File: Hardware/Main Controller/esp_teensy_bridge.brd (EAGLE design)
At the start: 99.7 x 88.3 mm, 47 parts, among them IC1 BQ79600PWRQ1, Q1 SI7611DN-T1-GE3, Q2 SI7611DN-T1-GE3, Q3 SI7611DN-T1-GE3, Q4 SI7611DN-T1-GE3

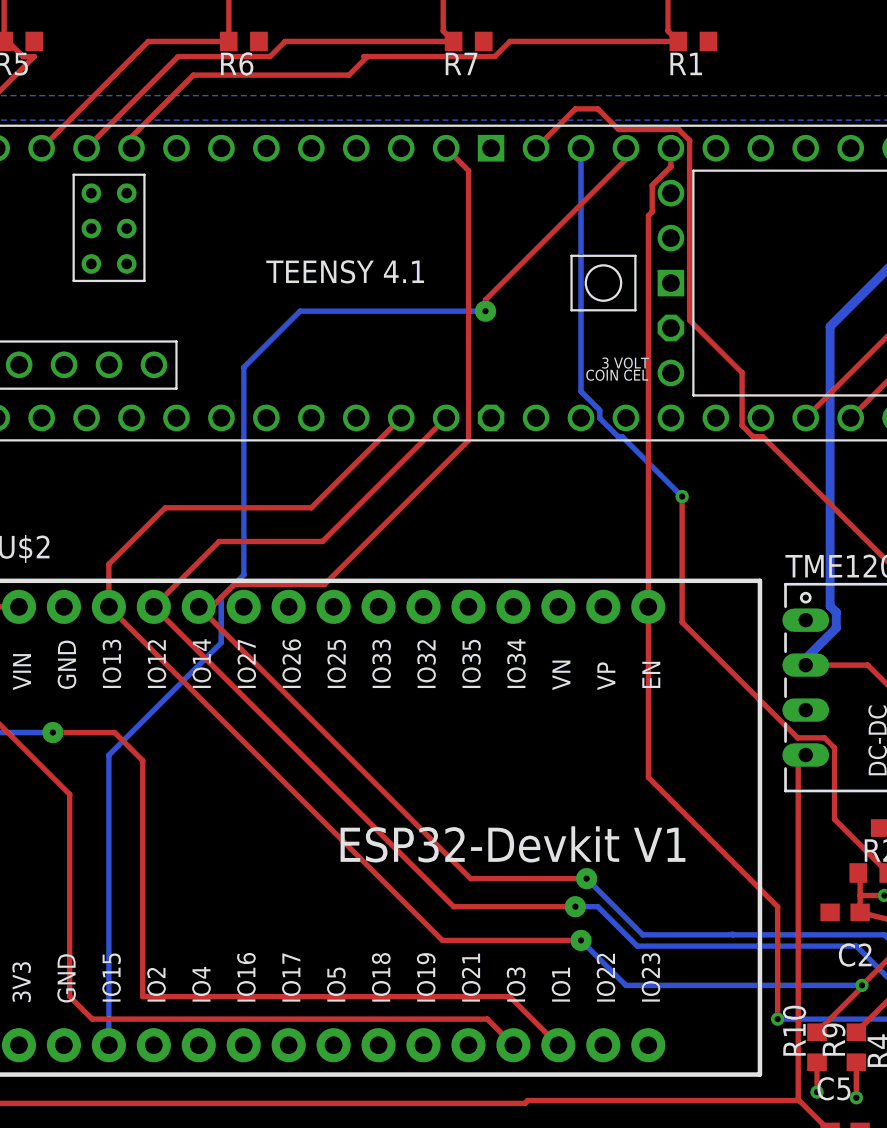
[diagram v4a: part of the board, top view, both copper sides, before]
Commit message: seperate spi
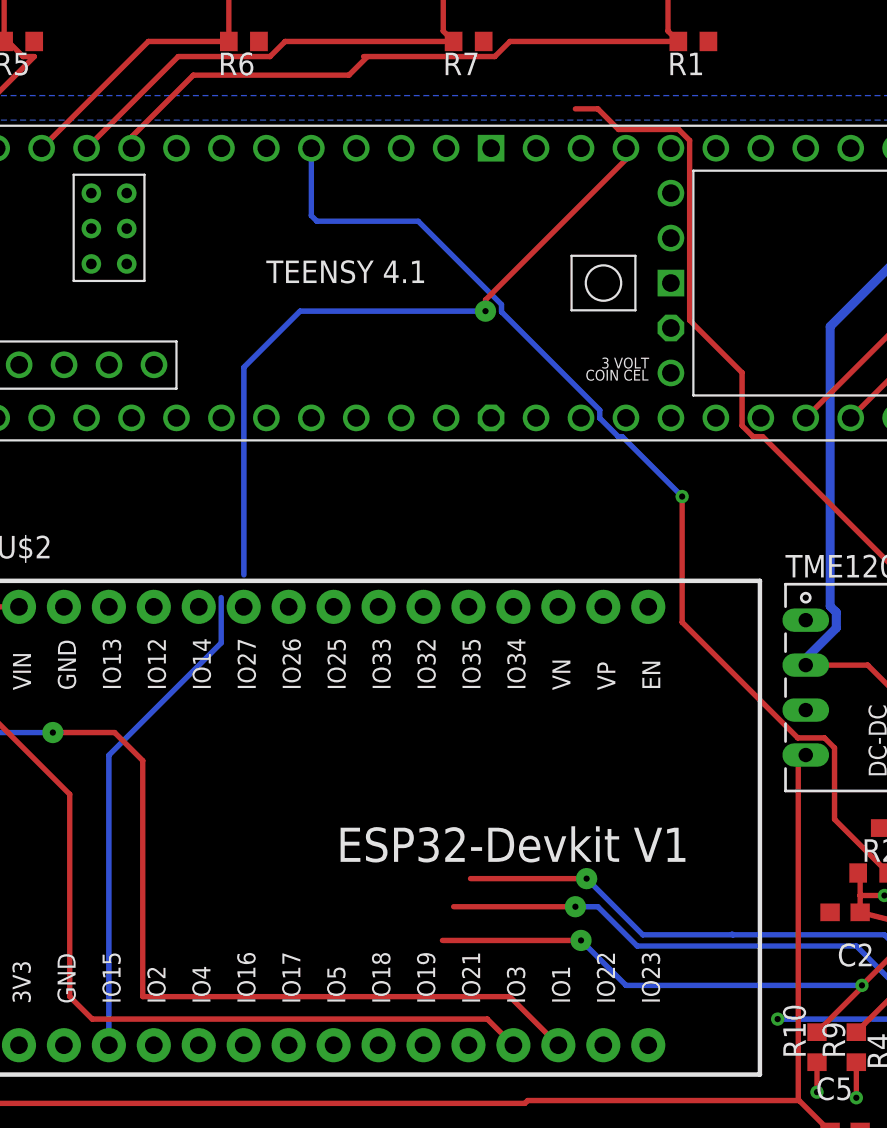
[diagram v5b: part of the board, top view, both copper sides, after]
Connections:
- removed net RX_BRIDGE: U$3.29-TX7
- removed net TX_BRIDGE: U$3.28-RX7
- new net MISO_ESP: U$2.27, U$3.41-A17/MISO1
- new net MOSI_ESP: U$2.28, U$3.26-A12/MOSI1
- new net SCK_ESP: U$2.26, U$3.27-A13/SCK1
- net MISO: no longer U$2.27
- net MOSI: no longer U$2.28
- net NFAULT: now also U$3.16-A2/RX4/SCL1; no longer U$3.40-A16/CS1
- net SCK: no longer U$2.26
- net SPI_RDY: now also U$3.17-A3/TX4/SDA1; no longer U$3.41-A17/MISO1
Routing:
- net SCK: track 87.8 -> 29.9 mm
- net CS0: track 66.1 -> 13.3 mm
- net MOSI: track 84.2 -> 35.1 mm
- net MISO: track 80.5 -> 35.6 mm
- net NFAULT: track 54.4 -> 64.0 mm
- net SPI_RDY: track 68.0 -> 64.8 mm
- net CS1: track 68.9 -> 67.1 mm
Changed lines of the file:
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@@
 <wire x1="14.9225" y1="13.335" x2="37.25" y2="13.335" width="0.3048" layer="1"/>
-</signal>
-<signal name="TX_BRIDGE">
-<contactref element="U$3" pad="28-RX7"/>
-</signal>
-<signal name="RX_BRIDGE">
-<contactref element="U$3" pad="29-TX7"/>
 </signal>
 <signal name="5V">
@@
 <contactref element="IC1" pad="4"/>
 <contactref element="U$3" pad="11-MOSI/CTX1"/>
-<contactref element="U$2" pad="28"/>
 <via x="58.42" y="15.24" extent="1-16" drill="0.35"/>
 <wire x1="58.42" y1="15.24" x2="60.9675" y2="17.7875" width="0.3048" layer="1"/>
@@
 <wire x1="55.88" y1="12.5975" x2="58.42" y2="15.1375" width="0.3048" layer="1"/>
 <wire x1="58.42" y1="15.1375" x2="58.42" y2="15.24" width="0.3048" layer="1"/>
-<wire x1="32.385" y1="47.3075" x2="27.305" y2="42.2275" width="0.3048" layer="1"/>
-<wire x1="27.305" y1="42.2275" x2="19.05" y2="42.2275" width="0.3048" layer="1"/>
-<wire x1="19.05" y1="42.2275" x2="15.865" y2="39.0425" width="0.3048" layer="1"/>
-<wire x1="15.865" y1="39.0425" x2="15.865" y2="36.63" width="0.3048" layer="1"/>
 <wire x1="45.085" y1="15.24" x2="42.545" y2="17.78" width="0.3048" layer="16"/>
 <via x="42.545" y="17.78" extent="1-16" drill="0.35" diameter="1.2"/>
-<wire x1="34.715" y1="17.78" x2="15.865" y2="36.63" width="0.3048" layer="1"/>
 <wire x1="58.42" y1="15.24" x2="45.085" y2="15.24" width="0.3048" layer="16"/>
 <wire x1="42.545" y1="17.78" x2="34.715" y2="17.78" width="0.3048" layer="1"/>
+<wire x1="34.715" y1="17.78" x2="32.385" y2="47.3075" width="0" layer="19" extent="1-1"/>
 </signal>
 <signal name="MISO">
 <contactref element="IC1" pad="5"/>
 <contactref element="U$3" pad="12-MISO/MQSL"/>
-<contactref element="U$2" pad="27"/>
 <wire x1="60.325" y1="15.24" x2="58.1025" y2="17.4625" width="0.3048" layer="16"/>
 <via x="60.325" y="15.24" extent="1-16" drill="0.35"/>
@@
 <via x="42.2275" y="19.685" extent="1-16" drill="0.35" diameter="1.2"/>
 <wire x1="42.2275" y1="19.685" x2="35.35" y2="19.685" width="0.3048" layer="1"/>
-<wire x1="35.35" y1="19.685" x2="18.405" y2="36.63" width="0.3048" layer="1"/>
-<wire x1="18.405" y1="36.63" x2="22.0975" y2="40.3225" width="0.3048" layer="1"/>
-<wire x1="22.0975" y1="40.3225" x2="27.94" y2="40.3225" width="0.3048" layer="1"/>
-<wire x1="27.94" y1="40.3225" x2="34.925" y2="47.3075" width="0.3048" layer="1"/>
+<wire x1="35.35" y1="19.685" x2="34.925" y2="47.3075" width="0" layer="19" extent="1-1"/>
 </signal>
 <signal name="SCK">
 <contactref element="IC1" pad="6"/>
 <contactref element="U$3" pad="13-SCK/LED"/>
-<contactref element="U$2" pad="26"/>
 <wire x1="51.0829125" y1="18.1455" x2="51.1309125" y2="18.0975" width="0.3048" layer="16"/>
 <wire x1="59.69" y1="18.0975" x2="61.2775" y2="16.51" width="0.3048" layer="16"/>
@@
 <via x="42.8625" y="21.2725" extent="1-16" drill="0.35" diameter="1.2"/>
 <wire x1="42.8625" y1="21.2725" x2="36.3025" y2="21.2725" width="0.3048" layer="1"/>
-<wire x1="36.3025" y1="21.2725" x2="20.945" y2="36.63" width="0.3048" layer="1"/>
 <wire x1="46.0375" y1="18.0975" x2="42.8625" y2="21.2725" width="0.3048" layer="16"/>
-<wire x1="28.0575" y1="37.9" x2="36.195" y2="46.0375" width="0.3048" layer="1"/>
-<wire x1="20.945" y1="36.63" x2="21.68894375" y2="36.63" width="0.3048" layer="1"/>
-<wire x1="21.68894375" y1="36.63" x2="22.95894375" y2="37.9" width="0.3048" layer="1"/>
-<wire x1="22.95894375" y1="37.9" x2="28.0575" y2="37.9" width="0.3048" layer="1"/>
-<wire x1="36.195" y1="46.0375" x2="36.195" y2="61.2775" width="0.3048" layer="1"/>
-<wire x1="36.195" y1="61.2775" x2="34.925" y2="62.5475" width="0.3048" layer="1"/>
+<wire x1="36.3025" y1="21.2725" x2="34.925" y2="62.5475" width="0" layer="19" extent="1-1"/>
 </signal>
 <signal name="CS1">
@@
 <via x="37.1475" y="53.34" extent="1-16" drill="0.35" diameter="1.2"/>
 <wire x1="37.1475" y1="53.34" x2="26.67" y2="53.34" width="0.3048" layer="16"/>
-<wire x1="23.495" y1="38.43605625" x2="22.215" y2="37.15605625" width="0.3048" layer="16"/>
 <wire x1="22.215" y1="37.15605625" x2="22.215" y2="34.5975" width="0.3048" layer="16"/>
 <wire x1="15.865" y1="28.2475" x2="15.865" y2="11.86" width="0.3048" layer="16"/>
@@
 <wire x1="23.495" y1="50.165" x2="23.495" y2="38.43605625" width="0.3048" layer="16"/>
 <wire x1="22.215" y1="34.5975" x2="15.865" y2="28.2475" width="0.3048" layer="16"/>
+<wire x1="22.215" y1="37.15605625" x2="23.495" y2="38.43605625" width="0" layer="19" extent="16-16"/>
 </signal>
 <signal name="CS0">
 <contactref element="U$3" pad="38-A14/CS/IN1"/>
 <contactref element="IC1" pad="7"/>
-<wire x1="47.625" y1="62.5475" x2="47.625" y2="61.504875" width="0.3048" layer="1"/>
-<wire x1="46.5662" y1="58.9487" x2="46.355" y2="58.7375" width="0.3048" layer="1"/>
-<wire x1="47.625" y1="61.504875" x2="46.5662" y2="60.446075" width="0.3048" layer="1"/>
-<wire x1="46.5662" y1="60.446075" x2="46.5662" y2="58.9487" width="0.3048" layer="1"/>
-<wire x1="46.355" y1="58.7375" x2="46.355" y2="26.9875" width="0.3048" layer="1"/>
-<wire x1="46.355" y1="26.9875" x2="53.6575" y2="19.685" width="0.3048" layer="1"/>
-<wire x1="53.6575" y1="19.685" x2="53.6575" y2="13.335" width="0.3048" layer="1"/>
 <via x="53.6575" y="13.335" extent="1-16" drill="0.35"/>
 <wire x1="53.6575" y1="13.335" x2="61.2775" y2="13.335" width="0.3048" layer="16"/>
@@
 <wire x1="60.6425" y1="11.9625" x2="60.6425" y2="12.7" width="0.3048" layer="1"/>
 <wire x1="60.6425" y1="12.7" x2="61.2775" y2="13.335" width="0.3048" layer="1"/>
+<wire x1="64.0545" y1="15.8375" x2="47.625" y2="62.5475" width="0" layer="19" extent="1-1"/>
 </signal>
 <signal name="NFAULT">
@@
 <wire x1="64.0545" y1="19.0875" x2="62.4075" y2="19.0875" width="0.3048" layer="1"/>
 <wire x1="62.4075" y1="19.0875" x2="59.905" y2="21.59" width="0.3048" layer="1"/>
-<contactref element="U$3" pad="40-A16/CS1"/>
 <via x="48.26" y="42.8625" extent="1-16" drill="0.35"/>
 <wire x1="56.8706" y1="28.6573" x2="56.3052" y2="29.2227" width="0.3048" layer="1"/>
@@
 <wire x1="48.26" y1="42.8625" x2="44.8738" y2="46.2487" width="0.3048" layer="16"/>
 <wire x1="44.8738" y1="46.2487" x2="44.646425" y2="46.2487" width="0.3048" layer="16"/>
-<wire x1="42.545" y1="48.804875" x2="42.545" y2="62.5475" width="0.3048" layer="16"/>
-<wire x1="43.6038" y1="47.746075" x2="42.545" y2="48.804875" width="0.3048" layer="16"/>
 <wire x1="44.646425" y1="46.2487" x2="43.6038" y2="47.291325" width="0.3048" layer="16"/>
 <wire x1="43.6038" y1="47.291325" x2="43.6038" y2="47.746075" width="0.3048" layer="16"/>
+<contactref element="U$3" pad="16-A2/RX4/SCL1"/>
+<wire x1="38.0523" y1="53.297575" x2="38.0523" y2="53.71478125" width="0.3048" layer="16"/>
+<wire x1="38.0523" y1="53.71478125" x2="33.34708125" y2="58.42" width="0.3048" layer="16"/>
+<wire x1="33.34708125" y1="58.42" x2="27.6225" y2="58.42" width="0.3048" layer="16"/>
+<wire x1="27.6225" y1="58.42" x2="27.305" y2="58.7375" width="0.3048" layer="16"/>
+<wire x1="27.305" y1="58.7375" x2="27.305" y2="62.5475" width="0.3048" layer="16"/>
+<wire x1="43.6038" y1="47.746075" x2="38.0523" y2="53.297575" width="0.3048" layer="16"/>
 </signal>
 <signal name="SPI_RDY">
@@
 <wire x1="63.5" y1="13.55" x2="63.5" y2="14.633" width="0.3048" layer="1"/>
 <wire x1="63.5" y1="14.633" x2="64.0545" y2="15.1875" width="0.3048" layer="1"/>
-<contactref element="U$3" pad="41-A17/MISO1"/>
 <wire x1="64.91825" y1="15.3077" x2="65.0968" y2="15.48625" width="0.3048" layer="1"/>
 <wire x1="62.6041" y1="35.0222125" x2="62.6041" y2="36.4559" width="0.3048" layer="1"/>
@@
 <wire x1="48.063575" y1="63.6063" x2="44.6612" y2="63.6063" width="0.3048" layer="1"/>
 <wire x1="43.4975" y1="64.77" x2="42.2275" y2="64.77" width="0.3048" layer="1"/>
-<wire x1="42.2275" y1="64.77" x2="40.005" y2="62.5475" width="0.3048" layer="1"/>
 <wire x1="62.6041" y1="36.4559" x2="52.8113" y2="46.2487" width="0.3048" layer="1"/>
+<contactref element="U$3" pad="17-A3/TX4/SDA1"/>
+<wire x1="42.2275" y1="64.77" x2="24.765" y2="62.5475" width="0" layer="19" extent="1-1"/>
+</signal>
+<signal name="MOSI_ESP">
+<contactref element="U$3" pad="26-A12/MOSI1"/>
+<contactref element="U$2" pad="28"/>
+<wire x1="15.865" y1="36.63" x2="45.085" y2="47.3075" width="0" layer="19" extent="1-1"/>
+</signal>
+<signal name="MISO_ESP">
+<contactref element="U$3" pad="41-A17/MISO1"/>
+<contactref element="U$2" pad="27"/>
+<wire x1="18.405" y1="36.63" x2="40.005" y2="62.5475" width="0" layer="19" extent="1-1"/>
+</signal>
+<signal name="SCK_ESP">
+<contactref element="U$3" pad="27-A13/SCK1"/>
+<contactref element="U$2" pad="26"/>
+<wire x1="20.945" y1="36.63" x2="47.625" y2="47.3075" width="0" layer="19" extent="1-1"/>
 </signal>
 </signals>

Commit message: 1/19/2022 changes josh/isaac
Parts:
- moved PWR_IN 23.6 mm to (61.6, 81.3)
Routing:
- net CS0: track 13.3 -> 65.9 mm
- net SCK: track 29.9 -> 77.3 mm, vias 2 -> 4
- net SCK_ESP: track 0.00 -> 38.8 mm, vias 0 -> 1
- net MISO_ESP: track 0.00 -> 35.6 mm, vias 0 -> 1
- net MOSI_ESP: track 0.00 -> 33.8 mm, vias 0 -> 3
- net GND: track 0.00 -> 31.2 mm, vias 0 -> 5
- net MOSI: track 35.1 -> 65.6 mm
- net MISO: track 35.6 -> 63.3 mm
- net VCC: track 143.0 -> 115.3 mm
- net SPI_RDY: track 64.8 -> 83.2 mm
- net CS1: track 67.1 -> 68.9 mm

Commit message: final additions hopefully
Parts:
- added LED1, LED2, LED3, LED4, LED5, LED6, LED7, LED8: (no value), led:SML0603
- added R11, R12, R13, R14: 100k, rcl:R0603
- added R15, R16, R17, R18: 50, rcl:R0603
- added X1: 5566-12, con-molex:5566-12
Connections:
- new net N$13: LED4.A, R14.2
- new net N$14: U$3.14-A0/TX3/SPDIF_OUT, X1.1
- new net N$17: U$3.15-A1/RX3/SPDIF_IN, X1.2
- new net N$18: U$3.18-A4/SDA0, X1.3
- new net N$19: U$3.19-A5/SCL0, X1.4
- new net N$20: U$3.24-A10/TX6/SCL2, X1.5
- new net N$21: U$3.25-A11/RX6/SDA2, X1.6
- new net N$22: U$3.40-A16/CS1, X1.7
- new net N$23: U$3.32-OUT1B, X1.8
- new net N$24: U$3.9-OUT1C, X1.9
- new net N$25: U$3.6-OUT1D, X1.10
- new net N$26: U$3.33-MCLK2, X1.12
- new net N$27: U$3.2-OUT2, X1.11
- new net N$28: R15.1, U$2.10
- new net N$29: R16.1, U$2.9
- new net N$3: LED1.A, R11.2
- new net N$30: R17.1, U$2.8
- new net N$31: R18.1, U$2.7
- new net N$32: LED5.A, R15.2
- new net N$33: LED6.A, R16.2
- new net N$34: LED7.A, R17.2
- new net N$35: LED8.A, R18.2
- new net N$4: LED2.A, R12.2
- new net N$9: LED3.A, R13.2
- net GND: now also LED1.C, LED2.C, LED3.C, LED4.C, LED5.C, LED6.C, LED7.C, LED8.C
- net N$12: now also R12.1
- net N$2: now also R13.1
- net N$5: now also R14.1
- net N$6: now also R11.1
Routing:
- net N$27: track 0.00 -> 89.1 mm, vias 0 -> 4
- net N$25: track 0.00 -> 71.5 mm, vias 0 -> 6
- net N$20: track 0.00 -> 70.9 mm, vias 0 -> 2
- net N$19: track 0.00 -> 69.8 mm
- net N$21: track 0.00 -> 66.1 mm, vias 0 -> 2
- net N$18: track 0.00 -> 62.3 mm
- net N$24: track 0.00 -> 58.9 mm, vias 0 -> 3
- net N$17: track 0.00 -> 49.1 mm, vias 0 -> 1
- net N$14: track 0.00 -> 41.6 mm, vias 0 -> 1
- net N$26: track 0.00 -> 39.9 mm
- net N$22: track 0.00 -> 31.3 mm, vias 0 -> 1
- net N$23: track 0.00 -> 23.9 mm
- net N$31: track 0.00 -> 5.93 mm, vias 0 -> 1
- net N$30: track 0.00 -> 5.93 mm, vias 0 -> 1
- net N$29: track 0.00 -> 5.93 mm, vias 0 -> 1
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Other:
- board text added: "CAN"
- board text added: "COMH"
- board text added: "COML"

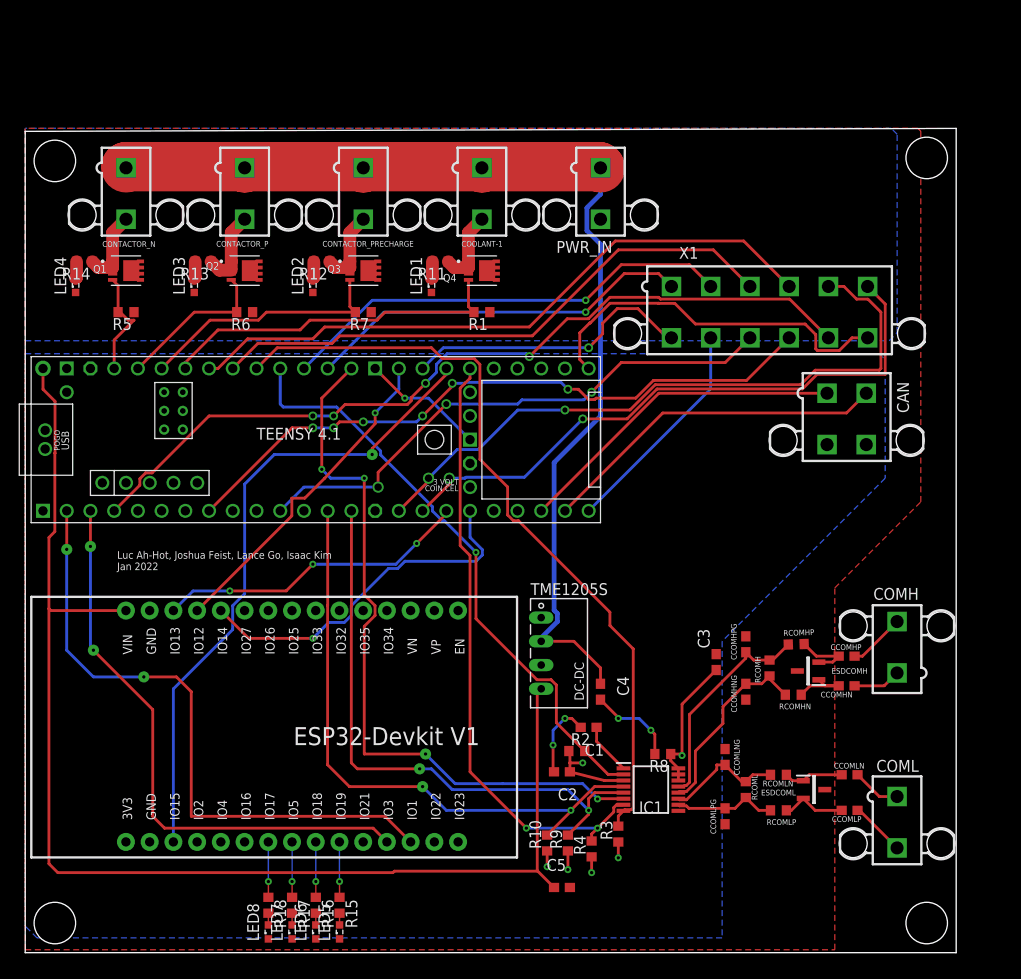
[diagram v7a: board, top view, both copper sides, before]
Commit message: Fixed MOSFETs
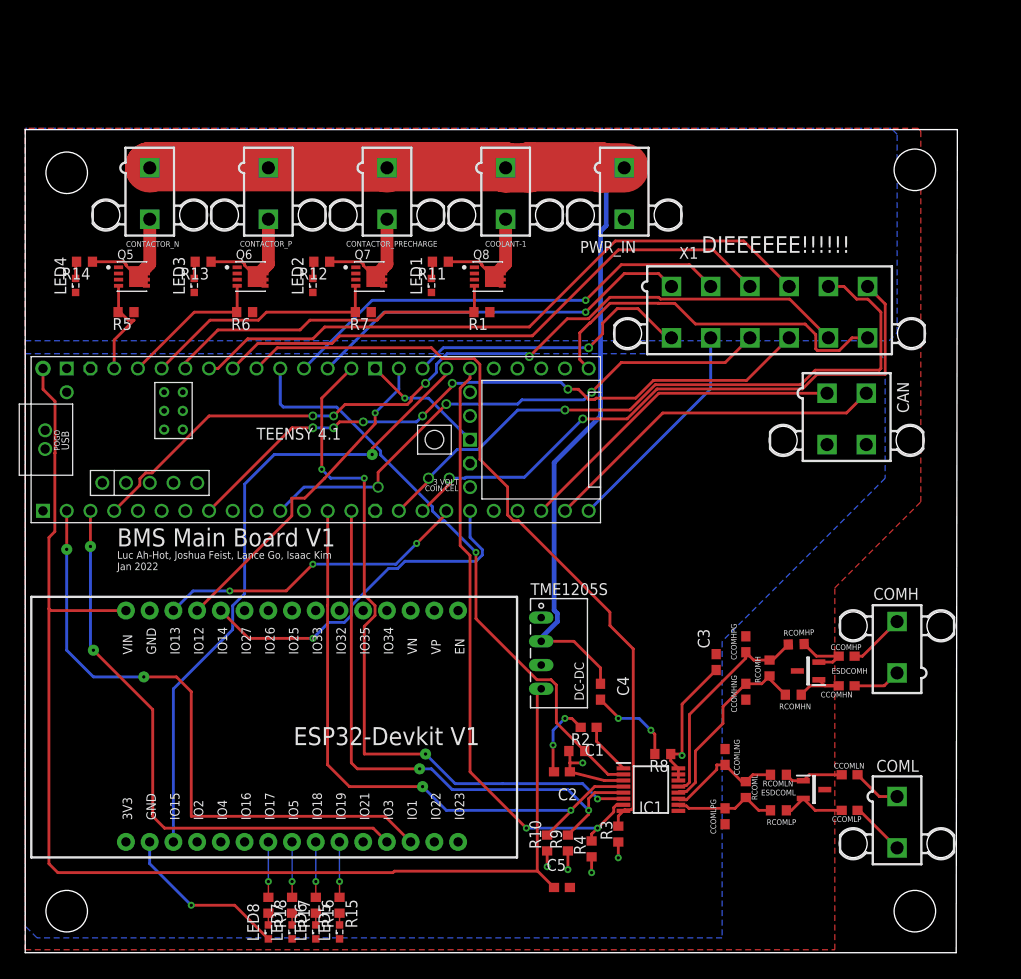
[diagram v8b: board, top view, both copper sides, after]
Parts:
- removed Q1, Q2, Q3, Q4: SI7611DN-T1-GE3, SI7611DN-T1-GE3:VISHAY_SIS468DN-T1-GE3
- added Q5, Q6, Q7, Q8: VISHAY_SIS862DN-T1-GE3VISHAY_SIS862DN-T1-GE3_0_0, Vishay - SIS862DN-T1-GE3:VISHAY_SIS862DN-T1-GE3_0
- moved PWR_IN 2.54 mm to (64.1, 81.3)
- moved CONTACTOR_N 2.54 mm to (13.3, 81.3)
- moved CONTACTOR_P 2.54 mm to (26.0, 81.3)
- moved CONTACTOR_PRECHARGE 2.54 mm to (38.7, 81.3)
- moved COOLANT-1 2.54 mm to (51.4, 81.3)
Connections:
- net CONTACTORN_CTRL: now also Q5.4; no longer Q1.4
- net CONTACTORPRECHARGE_CTRL: now also Q7.4; no longer Q3.4
- net CONTACTORP_CTRL: now also Q6.4; no longer Q2.4
- net COOLANT_CTRL: now also Q8.4; no longer Q4.4
- net GND: now also Q5.1, Q5.2, Q5.3, Q6.1, Q6.2, Q6.3, Q7.1, Q7.2, Q7.3, Q8.1, Q8.2, Q8.3; no longer Q1.5, Q1.6, Q1.7, Q1.8, Q1.9, Q2.5, Q2.6, Q2.7, Q2.8, Q2.9, Q3.5, Q3.6, Q3.7, Q3.8, Q3.9, Q4.5, Q4.6, Q4.7, Q4.8, Q4.9
- net N$12: now also Q7.5,6,7,8, Q7.5,6,7,8-2, Q7.5,6,7,8-3, Q7.5,6,7,8-4, Q7.5,6,7,8-5; no longer Q3.1, Q3.2, Q3.3
- net N$2: now also Q6.5,6,7,8, Q6.5,6,7,8-2, Q6.5,6,7,8-3, Q6.5,6,7,8-4, Q6.5,6,7,8-5; no longer Q2.1, Q2.2, Q2.3
- net N$5: now also Q5.5,6,7,8, Q5.5,6,7,8-2, Q5.5,6,7,8-3, Q5.5,6,7,8-4, Q5.5,6,7,8-5; no longer Q1.1, Q1.2, Q1.3
- net N$6: now also Q8.5,6,7,8, Q8.5,6,7,8-2, Q8.5,6,7,8-3, Q8.5,6,7,8-4, Q8.5,6,7,8-5; no longer Q4.1, Q4.2, Q4.3
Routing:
- net GND: track 31.2 -> 49.6 mm, vias 5 -> 6
- net N$12: track 8.85 -> 16.7 mm
- net N$2: track 8.96 -> 16.7 mm
- net N$5: track 8.85 -> 15.3 mm
- net N$6: track 8.85 -> 15.3 mm
- net VCC: track 115.3 -> 117.2 mm
- net COOLANT_CTRL: track 37.5 -> 36.6 mm
- net CONTACTORP_CTRL: track 16.8 -> 15.9 mm
- net CONTACTORN_CTRL: track 11.8 -> 11.0 mm
- net CONTACTORPRECHARGE_CTRL: track 26.9 -> 26.1 mm
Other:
- board size 99.7 x 88.3 mm -> 99.8 x 88.1 mm
- board text added: "DIEEEEEE!!!!!!"
